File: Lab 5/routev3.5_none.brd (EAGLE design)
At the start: 100 x 80 mm, 48 parts, among them J1 FTDI_DEVICERA_SMT, M1 WIRELESS-NRF24L01, U1 3.3V, U2 GY-521MPU6050

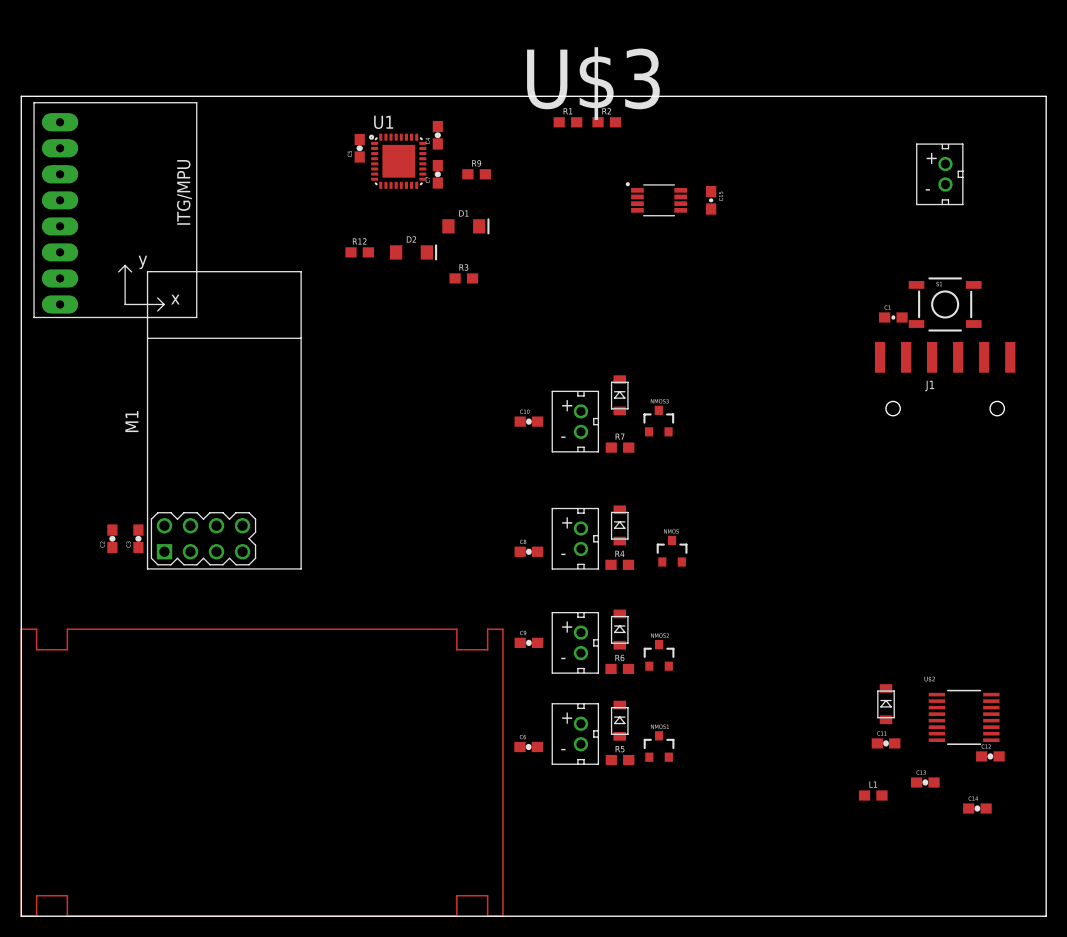
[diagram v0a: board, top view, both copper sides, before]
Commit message: Update template for cut-out - Latest route: routev3.5_vccgnd
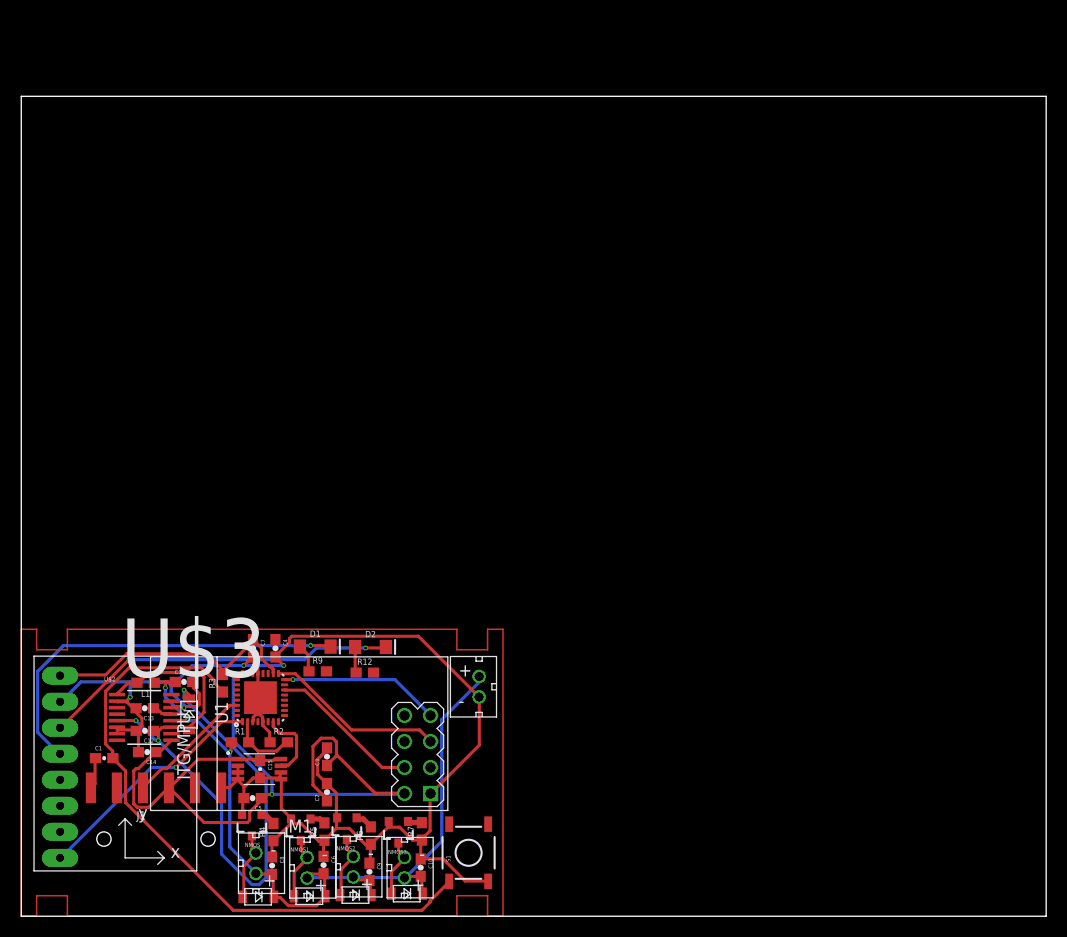
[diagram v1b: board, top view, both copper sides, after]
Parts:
- moved C1 88.2 mm to (8.09, 15.4)
- moved J1 87.7 mm to (13.1, 7.53)
- moved C12 82.5 mm to (12.1, 18.1), turned to 180 degrees
- moved C14 81.2 mm to (12.3, 16.0), turned to 180 degrees
- moved U$2 80.0 mm to (12.0, 19.4)
- moved C13 76.5 mm to (12.1, 20.3), turned to 180 degrees
- moved L1 71.8 mm to (12.1, 22.8), turned to 180 degrees
- moved S1 70.9 mm to (43.6, 6.19), turned to 90 degrees
- moved C15 70.8 mm to (23.3, 14.3)
- moved C11 68.8 mm to (15.9, 22.9)
- moved R1 68.4 mm to (21.3, 17.0)
- moved R2 68.4 mm to (25.1, 17.0)
- moved DIODE4 68.0 mm to (16.4, 19.7)
- moved U$3 67.8 mm to (23.2, 14.3)
- moved U$1 67.6 mm to (44.7, 22.4)
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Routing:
- net GND: track 0.00 -> 154.8 mm, vias 0 -> 4
- net VCC: track 0.00 -> 111.4 mm, vias 0 -> 2
- net BATTERY+: track 0.00 -> 80.3 mm, vias 0 -> 3
- net RESET: track 0.00 -> 62.4 mm
- net VR-PS: track 0.00 -> 50.3 mm, vias 0 -> 3
- net IMU-SDA: track 0.00 -> 38.8 mm, vias 0 -> 1
- net IMU-SCL: track 0.00 -> 35.1 mm, vias 0 -> 2
- net IMU-INT: track 0.00 -> 23.3 mm, vias 0 -> 1
- net RF-SCK: track 0.00 -> 17.6 mm
- net RF-MISO: track 0.00 -> 15.7 mm, vias 0 -> 1
- net N$1: track 0.00 -> 15.4 mm
- net RF-CSN: track 0.00 -> 14.8 mm
- net FTDI-RX: track 0.00 -> 12.5 mm
- net OSC1: track 0.00 -> 7.09 mm
- net N$6: track 0.00 -> 6.67 mm
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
